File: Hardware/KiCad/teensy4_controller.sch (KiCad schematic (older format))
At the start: 90 parts, among them J1 Screw_Terminal_01x04, J10 Conn_01x04, J11 Conn_01x03, J12 Conn_01x03, J13 Conn_01x03, J14 Conn_01x03, J15 Conn_01x02, J16 Conn_02x04_Odd_Even, J17 Conn_01x04, J18 Conn_01x04, J19 Conn_01x02, J2 Conn_01x05, J20 Screw_Terminal_01x02, J21 Screw_Terminal_01x02, J22 Conn_02x04_Odd_Even, J23 Conn_01x04, J24 Screw_Terminal_01x02, J25 Screw_Terminal_01x02, J26 Screw_Terminal_01x02, J27 Screw_Terminal_01x02, J28 Screw_Terminal_01x02, J29 Screw_Terminal_01x02, J3 Conn_01x05, J30 Screw_Terminal_01x02, J31 RJ45_Wiznet_RB1-125BAG1A, J4 Conn_01x05, J5 Conn_01x04, J6 Conn_01x04, J7 Conn_01x03, J8 Conn_01x02, J9 Conn_02x04_Odd_Even, U1 74LVC3G06, U2 74LVC3G06, U3 74LVC3G06, U4 MPXA6115A, U5 MPXA6115A, U6 Teensy4.1, U7 R-78E5.0-1.0, U8 ULN2003AD

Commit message: Update
As ordered
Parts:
- C1: value CP1 -> 47uF
- C5: footprint Resistor_SMD:R_0603_1608Metric_Pad1.05x0.95mm_HandSolder -> Capacitor_SMD:C_0603_1608Metric_Pad1.05x0.95mm_HandSolder
- J1: footprint TerminalBlock_Phoenix:TerminalBlock_Phoenix_MKDS-1,5-4-5.08_1x04_P5.08mm_Horizontal -> TerminalBlock_Phoenix:TerminalBlock_Phoenix_MKDS-1,5-4_1x04_P5.00mm_Horizontal
- U1, U2, U3: value 74LVC3G06 -> 74LVC3G07
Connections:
- net labels added: A_CS, A_DIR, A_ENABLE, A_M1, A_M2, A_M3, A_RST, A_SLP, A_STEP, B_CS, B_DIR, B_ENABLE, B_M1, B_M2, B_M3, B_RST, B_SLP, B_STEP, C_CS, C_DIR, C_ENABLE, C_M1, C_M2, C_M3, C_RST, C_SLP, C_STEP, MOT_A_CS, MOT_B_CS, MOT_C_CS
- net labels removed: MOT_X_CS, MOT_Y_CS, MOT_Z_CS, X_CS, X_M1, X_M2, X_M3, X_RST, X_SLP, Y_CS, Y_M1, Y_M2, Y_M3, Y_RST, Y_SLP, Z_CS, Z_M1, Z_M2, Z_M3, Z_RST, Z_SLP
- wire segments 372 -> 381
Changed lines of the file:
@@
 $EndDescr
 Text Label 6150 2100 0    50   ~ 0
-X_DIR
+A_DIR
 Text Label 6150 2200 0    50   ~ 0
-X_STEP
+A_STEP
 Text Label 6500 2500 2    50   ~ 0
-X_ENABLE
+A_ENABLE
 Text Label 6150 2800 0    50   ~ 0
-Y_DIR
+B_DIR
 Text Label 6150 2900 0    50   ~ 0
-Y_STEP
+B_STEP
 Text Label 6500 3500 2    50   ~ 0
-Y_ENABLE
+B_ENABLE
 Text Label 10350 3800 2    50   ~ 0
 Z_STOP
 Text Label 6150 3700 0    50   ~ 0
-Z_DIR
+C_DIR
 Text Label 6150 3800 0    50   ~ 0
-Z_STEP
+C_STEP
 Wire Wire Line
 	9350 3200 10400 3200
@@
 	6100 4100 7150 4100
 Text Label 6500 4100 2    50   ~ 0
-Z_ENABLE
+C_ENABLE
 Wire Wire Line
 	7150 1900 6950 1900
@@
 F 0 "J1" H 12818 8417 50  0000 C CNN
 F 1 "Screw_Terminal_01x04" H 12818 8326 50  0000 C CNN
-F 2 "TerminalBlock_Phoenix:TerminalBlock_Phoenix_MKDS-1,5-4-5.08_1x04_P5.08mm_Horizontal" H 12900 8100 50  0001 C CNN
+F 2 "TerminalBlock_Phoenix:TerminalBlock_Phoenix_MKDS-1,5-4_1x04_P5.00mm_Horizontal" H 12900 8100 50  0001 C CNN
 F 3 "~" H 12900 8100 50  0001 C CNN
 	1    12900 8100
@@
 P 2400 8000
 F 0 "C1" H 2515 8046 50  0000 L CNN
-F 1 "CP1" H 2515 7955 50  0000 L CNN
+F 1 "47uF" H 2515 7955 50  0000 L CNN
 F 2 "Capacitor_SMD:CP_Elec_6.3x7.7" H 2400 8000 50  0001 C CNN
 F 3 "~" H 2400 8000 50  0001 C CNN
@@
 	4600 8550 3550 8550
 Text Label 4150 8550 0    50   ~ 0
-X_STEP
+A_STEP
 Wire Wire Line
 	4600 8650 3550 8650
 Text Label 4150 8650 0    50   ~ 0
-X_DIR
+A_DIR
 Wire Wire Line
 	8000 8550 6950 8550
 Text Label 7550 8550 0    50   ~ 0
-Y_STEP
+B_STEP
 Wire Wire Line
 	8000 8650 6950 8650
 Text Label 7550 8650 0    50   ~ 0
-Y_DIR
+B_DIR
 Wire Wire Line
 	4600 8450 3550 8450
@@
 P 2750 1950
 F 0 "U1" H 2725 2217 50  0000 C CNN
-F 1 "74LVC3G06" H 2725 2126 50  0000 C CNN
+F 1 "74LVC3G07" H 2725 2126 50  0000 C CNN
 F 2 "Package_SO:VSSOP-8_3.0x3.0mm_P0.65mm" H 2750 1950 50  0001 C CNN
 F 3 "http://www.ti.com/lit/sg/scyt129e/scyt129e.pdf" H 2750 1950 50  0001 C CNN
@@
 P 2750 2400
 F 0 "U1" H 2725 2667 50  0000 C CNN
-F 1 "74LVC3G06" H 2725 2576 50  0000 C CNN
+F 1 "74LVC3G07" H 2725 2576 50  0000 C CNN
 F 2 "Package_SO:VSSOP-8_3.0x3.0mm_P0.65mm" H 2750 2400 50  0001 C CNN
 F 3 "http://www.ti.com/lit/sg/scyt129e/scyt129e.pdf" H 2750 2400 50  0001 C CNN
@@
 P 2750 3300
 F 0 "U2" H 2725 3567 50  0000 C CNN
-F 1 "74LVC3G06" H 2725 3476 50  0000 C CNN
+F 1 "74LVC3G07" H 2725 3476 50  0000 C CNN
 F 2 "Package_SO:VSSOP-8_3.0x3.0mm_P0.65mm" H 2750 3300 50  0001 C CNN
 F 3 "http://www.ti.com/lit/sg/scyt129e/scyt129e.pdf" H 2750 3300 50  0001 C CNN
@@
 P 2750 3750
 F 0 "U2" H 2725 4017 50  0000 C CNN
-F 1 "74LVC3G06" H 2725 3926 50  0000 C CNN
+F 1 "74LVC3G07" H 2725 3926 50  0000 C CNN
 F 2 "Package_SO:VSSOP-8_3.0x3.0mm_P0.65mm" H 2750 3750 50  0001 C CNN
 F 3 "http://www.ti.com/lit/sg/scyt129e/scyt129e.pdf" H 2750 3750 50  0001 C CNN
@@
 P 2750 4200
 F 0 "U2" H 2725 4467 50  0000 C CNN
-F 1 "74LVC3G06" H 2725 4376 50  0000 C CNN
+F 1 "74LVC3G07" H 2725 4376 50  0000 C CNN
 F 2 "Package_SO:VSSOP-8_3.0x3.0mm_P0.65mm" H 2750 4200 50  0001 C CNN
 F 3 "http://www.ti.com/lit/sg/scyt129e/scyt129e.pdf" H 2750 4200 50  0001 C CNN
@@
 P 2750 2850
 F 0 "U1" H 2725 3117 50  0000 C CNN
-F 1 "74LVC3G06" H 2725 3026 50  0000 C CNN
+F 1 "74LVC3G07" H 2725 3026 50  0000 C CNN
 F 2 "Package_SO:VSSOP-8_3.0x3.0mm_P0.65mm" H 2750 2850 50  0001 C CNN
 F 3 "http://www.ti.com/lit/sg/scyt129e/scyt129e.pdf" H 2750 2850 50  0001 C CNN
@@
 F 0 "C5" H 5915 6746 50  0000 L CNN
 F 1 "47pF" H 5915 6655 50  0000 L CNN
-F 2 "Resistor_SMD:R_0603_1608Metric_Pad1.05x0.95mm_HandSolder" H 5838 6550 50  0001 C CNN
+F 2 "Capacitor_SMD:C_0603_1608Metric_Pad1.05x0.95mm_HandSolder" H 5838 6550 50  0001 C CNN
 F 3 "~" H 5800 6700 50  0001 C CNN
 	1    5800 6700
@@
 	11400 8550 10350 8550
 Text Label 10950 8550 0    50   ~ 0
-Z_STEP
+C_STEP
 Wire Wire Line
 	11400 8650 10350 8650
 Text Label 10950 8650 0    50   ~ 0
-Z_DIR
+C_DIR
 Wire Wire Line
 	11400 8450 10350 8450
 Text Label 10950 8450 0    50   ~ 0
-Z_ENABLE
+C_ENABLE
 $Comp
 L Connector_Generic:Conn_01x04 J18
@@
 P 2750 5550
 F 0 "U3" H 2725 5817 50  0000 C CNN
-F 1 "74LVC3G06" H 2725 5726 50  0000 C CNN
+F 1 "74LVC3G07" H 2725 5726 50  0000 C CNN
 F 2 "Package_SO:VSSOP-8_3.0x3.0mm_P0.65mm" H 2750 5550 50  0001 C CNN
 F 3 "http://www.ti.com/lit/sg/scyt129e/scyt129e.pdf" H 2750 5550 50  0001 C CNN
@@
 P 2750 4650
 F 0 "U3" H 2725 4917 50  0000 C CNN
-F 1 "74LVC3G06" H 2725 4826 50  0000 C CNN
+F 1 "74LVC3G07" H 2725 4826 50  0000 C CNN
 F 2 "Package_SO:VSSOP-8_3.0x3.0mm_P0.65mm" H 2750 4650 50  0001 C CNN
 F 3 "http://www.ti.com/lit/sg/scyt129e/scyt129e.pdf" H 2750 4650 50  0001 C CNN
@@
 P 2750 5100
 F 0 "U3" H 2725 5367 50  0000 C CNN
-F 1 "74LVC3G06" H 2725 5276 50  0000 C CNN
+F 1 "74LVC3G07" H 2725 5276 50  0000 C CNN
 F 2 "Package_SO:VSSOP-8_3.0x3.0mm_P0.65mm" H 2750 5100 50  0001 C CNN
 F 3 "http://www.ti.com/lit/sg/scyt129e/scyt129e.pdf" H 2750 5100 50  0001 C CNN
@@
 SCK
 Text Label 7550 8450 0    50   ~ 0
-Y_ENABLE
+B_ENABLE
 Text Label 4150 8450 0    50   ~ 0
-X_ENABLE
+A_ENABLE
 Text Label 3300 5550 0    50   ~ 0
 Z_ENABLE
@@
 	2850 10000 3200 10000
 Text Label 2950 10000 0    50   ~ 0
-X_M1
+A_M1
 Wire Wire Line
 	2850 10100 3200 10100
 Text Label 2950 10100 0    50   ~ 0
-X_M2
+A_M2
 Wire Wire Line
 	2850 10200 3200 10200
 Text Label 2950 10200 0    50   ~ 0
-X_M3
+A_M3
 Wire Wire Line
 	2850 10300 3200 10300
 Text Label 2950 10300 0    50   ~ 0
-X_RST
+A_RST
 Text Label 3750 10300 0    50   ~ 0
-X_SLP
+A_SLP
 Wire Wire Line
 	3550 8850 3900 8850
 Text Label 3650 8850 0    50   ~ 0
-X_M1
+A_M1
 Wire Wire Line
 	3550 8950 3900 8950
 Text Label 3650 8950 0    50   ~ 0
-X_M2
+A_M2
 Wire Wire Line
 	3550 9050 3900 9050
 Text Label 3650 9050 0    50   ~ 0
-X_M3
+A_M3
 Wire Wire Line
 	3550 8150 3900 8150
 Text Label 3650 8150 0    50   ~ 0
-X_RST
+A_RST
 Wire Wire Line
 	3550 8250 3900 8250
 Text Label 3650 8250 0    50   ~ 0
-X_SLP
+A_SLP
 Text Label 1900 10000 0    50   ~ 0
 MOT_MOSI
@@
 	2350 10300 1850 10300
 Text Label 1900 10300 0    50   ~ 0
-MOT_X_CS
+MOT_A_CS
 $Comp
 L Connector_Generic:Conn_01x04 J17
@@
 	6250 10000 6600 10000
 Text Label 6350 10000 0    50   ~ 0
-Y_M1
+B_M1
 Wire Wire Line
 	6250 10100 6600 10100
 Text Label 6350 10100 0    50   ~ 0
-Y_M2
+B_M2
 Wire Wire Line
 	6250 10200 6600 10200
 Text Label 6350 10200 0    50   ~ 0
-Y_M3
+B_M3
 Wire Wire Line
 	6250 10300 6600 10300
 Text Label 6350 10300 0    50   ~ 0
-Y_RST
+B_RST
 Text Label 7150 10300 0    50   ~ 0
-Y_SLP
+B_SLP
 Text Label 5300 10000 0    50   ~ 0
 MOT_MOSI
@@
 	5750 10300 5250 10300
 Text Label 5300 10300 0    50   ~ 0
-MOT_Y_CS
+MOT_B_CS
 $Comp
 L Connector_Generic:Conn_01x04 J23
@@
 	9650 10000 10000 10000
 Text Label 9750 10000 0    50   ~ 0
-Z_M1
+C_M1
 Wire Wire Line
 	9650 10100 10000 10100
 Text Label 9750 10100 0    50   ~ 0
-Z_M2
+C_M2
 Wire Wire Line
 	9650 10200 10000 10200
 Text Label 9750 10200 0    50   ~ 0
-Z_M3
+C_M3
 Wire Wire Line
 	9650 10300 10000 10300
 Text Label 9750 10300 0    50   ~ 0
-Z_RST
+C_RST
 Text Label 10550 10300 0    50   ~ 0
-Z_SLP
+C_SLP
 Text Label 8700 10000 0    50   ~ 0
 MOT_MOSI
@@
 	9150 10300 8650 10300
 Text Label 8700 10300 0    50   ~ 0
-MOT_Z_CS
+MOT_C_CS
 Wire Wire Line
 	9950 7850 10850 7850
@@
 	6950 8150 7300 8150
 Text Label 7050 8150 0    50   ~ 0
-Y_RST
+B_RST
 Wire Wire Line
 	6950 8250 7300 8250
 Text Label 7050 8250 0    50   ~ 0
-Y_SLP
+B_SLP
 Wire Wire Line
 	10350 8150 10700 8150
 Text Label 10450 8150 0    50   ~ 0
-Z_RST
+C_RST
 Wire Wire Line
 	10350 8250 10700 8250
 Text Label 10450 8250 0    50   ~ 0
-Z_SLP
+C_SLP
 Wire Wire Line
 	6950 8850 7300 8850
 Text Label 7050 8850 0    50   ~ 0
-Y_M1
+B_M1
 Wire Wire Line
 	6950 8950 7300 8950
 Text Label 7050 8950 0    50   ~ 0
-Y_M2
+B_M2
 Wire Wire Line
 	6950 9050 7300 9050
 Text Label 7050 9050 0    50   ~ 0
-Y_M3
+B_M3
 Wire Wire Line
 	10350 8850 10700 8850
 Text Label 10450 8850 0    50   ~ 0
-Z_M1
+C_M1
 Wire Wire Line
 	10350 8950 10700 8950
 Text Label 10450 8950 0    50   ~ 0
-Z_M2
+C_M2
 Wire Wire Line
 	10350 9050 10700 9050
 Text Label 10450 9050 0    50   ~ 0
-Z_M3
+C_M3
 $Comp
 L Device:R R4
@@
 	7150 2700 6100 2700
 Text Label 6150 2700 0    50   ~ 0
-Y_CS
+B_CS
 $Comp
 L Device:R R10
@@
 	7150 2000 6100 2000
 Text Label 6150 2000 0    50   ~ 0
-X_CS
+A_CS
 $Comp
 L Device:R R9
@@
 	7150 3600 6100 3600
 Text Label 6150 3600 0    50   ~ 0
-Z_CS
+C_CS
 $Comp
 L Device:R R11
@@
 	5800 2000 5100 2000
 Text Label 5500 2000 2    50   ~ 0
-MOT_X_CS
+MOT_A_CS
 Wire Wire Line
 	5800 2700 5100 2700
 Text Label 5500 2700 2    50   ~ 0
-MOT_Y_CS
+MOT_B_CS
 Wire Wire Line
 	5800 3600 5100 3600
 Text Label 5500 3600 2    50   ~ 0
-MOT_Z_CS
+MOT_C_CS
 $Comp
 L Connector_Generic:Conn_01x02 J15
@@
 	13100 5250 12650 5250
 Connection ~ 13100 5500
+Text Label 6150 2300 0    50   ~ 0
+X_DIR
+Text Label 6150 2400 0    50   ~ 0
+X_STEP
+Wire Wire Line
+	6100 2300 7150 2300
+Wire Wire Line
+	6100 2400 7150 2400
+Text Label 6150 3000 0    50   ~ 0
+Y_DIR
+Text Label 6150 3400 0    50   ~ 0
+Y_STEP
+Wire Wire Line
+	6100 3000 7150 3000
+Wire Wire Line
+	6100 3400 7150 3400
+Text Label 6150 3900 0    50   ~ 0
+Z_DIR
+Text Label 6150 4000 0    50   ~ 0
+Z_STEP
+Wire Wire Line
+	6100 3900 7150 3900
+Wire Wire Line
+	6100 4000 7150 4000
+Wire Wire Line
+	9350 2200 10400 2200
+Text Label 10000 2200 0    50   ~ 0
+Y_ENABLE
+Wire Wire Line
+	9350 2300 10400 2300
+Text Label 10000 2300 0    50   ~ 0
+Z_ENABLE
+Text Label 6500 2600 2    50   ~ 0
+X_ENABLE
+Wire Wire Line
+	7150 2600 6100 2600
 $EndSCHEMATC

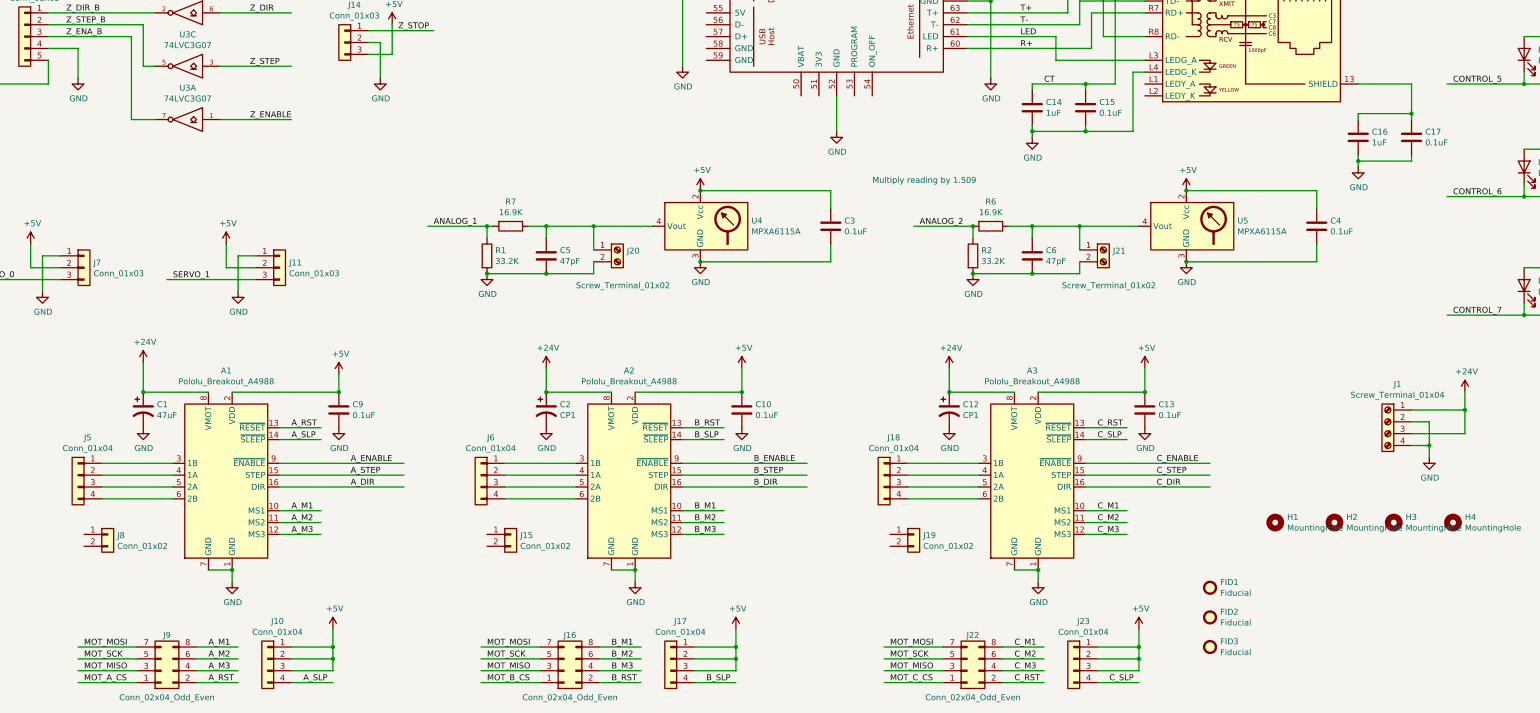
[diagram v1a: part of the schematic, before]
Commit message: Correct error on TMC SPI connections
MISO and CS were swapped at config jumpers
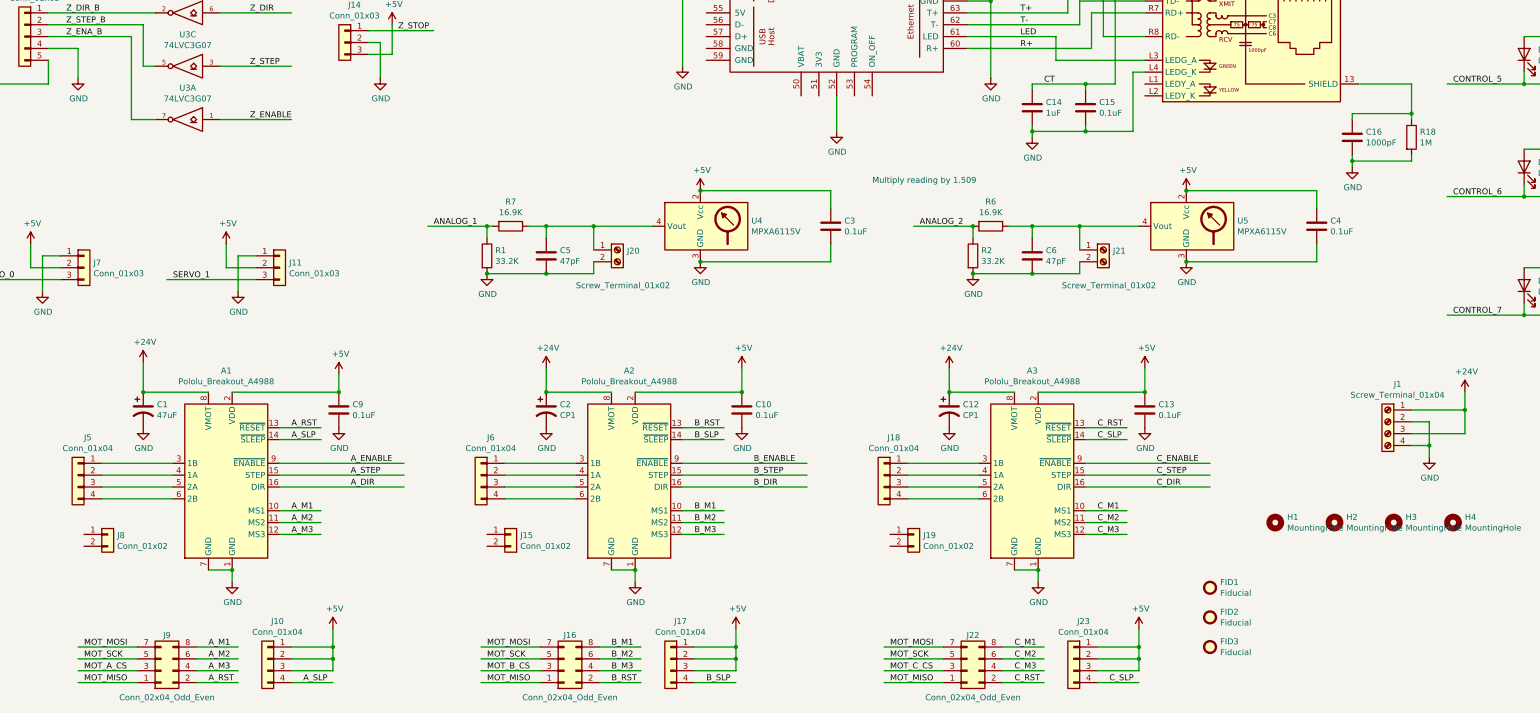
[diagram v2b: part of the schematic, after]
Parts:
- removed C17: 0.1uF, Capacitor_SMD:C_0603_1608Metric_Pad1.05x0.95mm_HandSolder, symbol Device:C
- added R18: 1M, Resistor_SMD:R_0603_1608Metric_Pad1.05x0.95mm_HandSolder, symbol Device:R
- C16: value 1uF -> 1000pF
- U4, U5: value MPXA6115A -> MPXA6115V
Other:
- moved on the sheet: C16
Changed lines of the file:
@@
 P 7100 6450
 F 0 "U4" H 6670 6496 50  0000 R CNN
-F 1 "MPXA6115A" H 6670 6405 50  0000 R CNN
+F 1 "MPXA6115V" H 6670 6405 50  0000 R CNN
 F 2 "misc:MPXA6115A" H 6600 6100 50  0001 C CNN
 F 3 "http://www.nxp.com/files/sensors/doc/data_sheet/MPXA6115A.pdf" H 7100 7050 50  0001 C CNN
@@
 P 11200 6450
 F 0 "U5" H 10770 6496 50  0000 R CNN
-F 1 "MPXA6115A" H 10770 6405 50  0000 R CNN
+F 1 "MPXA6115V" H 10770 6405 50  0000 R CNN
 F 2 "misc:MPXA6115A" H 10700 6100 50  0001 C CNN
 F 3 "http://www.nxp.com/files/sensors/doc/data_sheet/MPXA6115A.pdf" H 11200 7050 50  0001 C CNN
@@
 	2350 10200 1850 10200
 Text Label 1900 10200 0    50   ~ 0
-MOT_MISO
+MOT_A_CS
 Wire Wire Line
 	2350 10300 1850 10300
 Text Label 1900 10300 0    50   ~ 0
-MOT_A_CS
+MOT_MISO
 $Comp
 L Connector_Generic:Conn_01x04 J17
@@
 	5750 10200 5250 10200
 Text Label 5300 10200 0    50   ~ 0
-MOT_MISO
+MOT_B_CS
 Wire Wire Line
 	5750 10300 5250 10300
 Text Label 5300 10300 0    50   ~ 0
-MOT_B_CS
+MOT_MISO
 $Comp
 L Connector_Generic:Conn_01x04 J23
@@
 	9150 10200 8650 10200
 Text Label 8700 10200 0    50   ~ 0
-MOT_MISO
+MOT_C_CS
 Wire Wire Line
 	9150 10300 8650 10300
 Text Label 8700 10300 0    50   ~ 0
-MOT_C_CS
+MOT_MISO
 Wire Wire Line
 	9950 7850 10850 7850
@@
 $EndComp
 $Comp
-L Device:C C17
-U 1 1 5F9CB2EA
-P 13100 5700
-F 0 "C17" H 13215 5746 50  0000 L CNN
-F 1 "0.1uF" H 13215 5655 50  0000 L CNN
-F 2 "Capacitor_SMD:C_0603_1608Metric_Pad1.05x0.95mm_HandSolder" H 13138 5550 50  0001 C CNN
-F 3 "~" H 13100 5700 50  0001 C CNN
-	1    13100 5700
-	1    0    0    -1
-$EndComp
-$Comp
 L Device:C C16
 U 1 1 5F9CB2F0
-P 12650 5700
-F 0 "C16" H 12765 5746 50  0000 L CNN
-F 1 "1uF" H 12765 5655 50  0000 L CNN
-F 2 "Capacitor_SMD:C_1210_3225Metric_Pad1.42x2.65mm_HandSolder" H 12688 5550 50  0001 C CNN
-F 3 "~" H 12650 5700 50  0001 C CNN
-	1    12650 5700
-	1    0    0    -1
-$EndComp
-Wire Wire Line
-	12650 5550 12650 5500
-Wire Wire Line
-	12650 5500 13100 5500
-Wire Wire Line
-	12650 5900 12650 5850
-Wire Wire Line
-	13100 5900 12650 5900
-Wire Wire Line
-	12650 5900 12650 5950
-Connection ~ 12650 5900
+P 12600 5700
+F 0 "C16" H 12715 5746 50  0000 L CNN
+F 1 "1000pF" H 12715 5655 50  0000 L CNN
+F 2 "Capacitor_SMD:C_1210_3225Metric_Pad1.42x2.65mm_HandSolder" H 12638 5550 50  0001 C CNN
+F 3 "~" H 12600 5700 50  0001 C CNN
+	1    12600 5700
+	1    0    0    -1
+$EndComp
+Wire Wire Line
+	12600 5550 12600 5500
+Wire Wire Line
+	12600 5500 13100 5500
+Wire Wire Line
+	12600 5900 12600 5850
+Wire Wire Line
+	13100 5900 12600 5900
+Wire Wire Line
+	12600 5900 12600 5950
+Connection ~ 12600 5900
 $Comp
 L power:GND #PWR0156
 U 1 1 5F9CB2FC
-P 12650 5950
-F 0 "#PWR0156" H 12650 5700 50  0001 C CNN
-F 1 "GND" H 12655 5777 50  0000 C CNN
-F 2 "" H 12650 5950 50  0001 C CNN
-F 3 "" H 12650 5950 50  0001 C CNN
-	1    12650 5950
-	1    0    0    -1
-$EndComp
-Wire Wire Line
-	13100 5550 13100 5500
+P 12600 5950
+F 0 "#PWR0156" H 12600 5700 50  0001 C CNN
+F 1 "GND" H 12605 5777 50  0000 C CNN
+F 2 "" H 12600 5950 50  0001 C CNN
+F 3 "" H 12600 5950 50  0001 C CNN
+	1    12600 5950
+	1    0    0    -1
+$EndComp
 Wire Wire Line
 	13100 5850 13100 5900
 Wire Wire Line
-	13100 5500 13100 5250
-Wire Wire Line
 	13100 5250 12650 5250
-Connection ~ 13100 5500
 Text Label 6150 2300 0    50   ~ 0
 X_DIR
@@
 Wire Wire Line
 	7150 2600 6100 2600
+Wire Wire Line
+	13100 5250 13100 5500
+Connection ~ 13100 5500
+Wire Wire Line
+	13100 5500 13100 5550
+$Comp
+L Device:R R18
+U 1 1 600EDD50
+P 13100 5700
+F 0 "R18" H 13170 5746 50  0000 L CNN
+F 1 "1M" H 13170 5655 50  0000 L CNN
+F 2 "Resistor_SMD:R_0603_1608Metric_Pad1.05x0.95mm_HandSolder" V 13030 5700 50  0001 C CNN
+F 3 "~" H 13100 5700 50  0001 C CNN
+	1    13100 5700
+	1    0    0    -1
+$EndComp
 $EndSCHEMATC
